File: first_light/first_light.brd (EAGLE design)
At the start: 100 x 50 mm, 50 parts, among them IC1 MC34063AD, J1 DCJ0202, J2 DCJ0202, Q1 ZXMN4A06GTA, T1 UM2222AU3T106, T2 UM2222AU3T106, T3 UM2222AU3T106, T4 UM2222AU3T106, T5 UM2222AU3T106, U1 ESP32-WROOM-32D

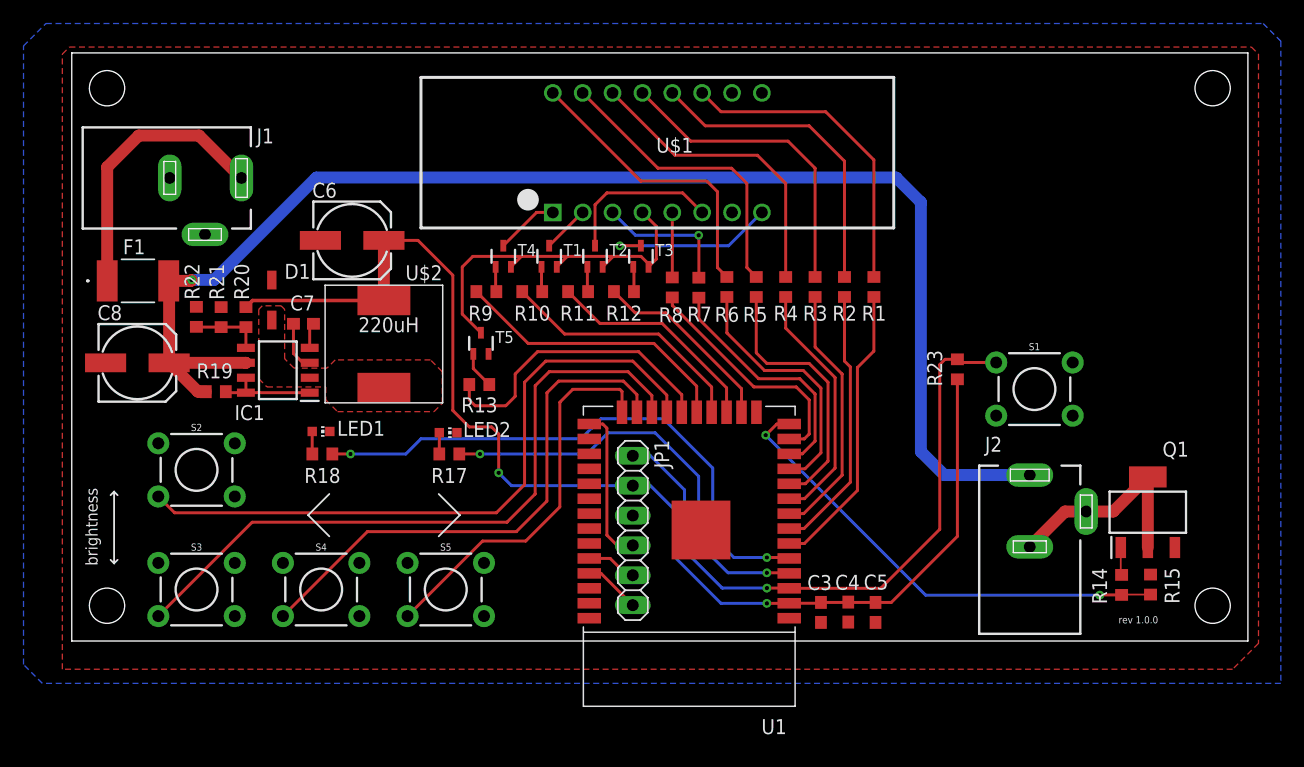
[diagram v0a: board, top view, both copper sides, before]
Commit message: added vias for a better ground plane and too fill between some tracks"
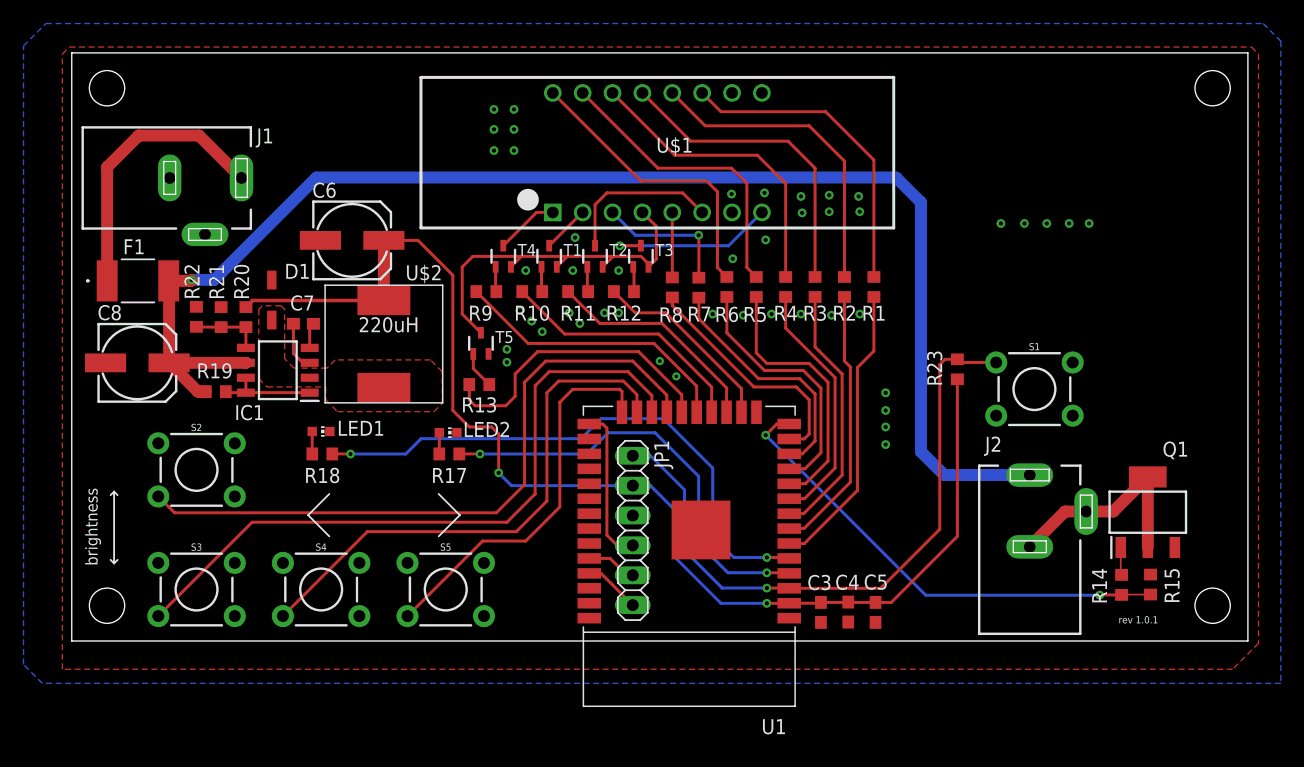
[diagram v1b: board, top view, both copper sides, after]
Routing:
- net GND: vias 0 -> 46
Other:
- board text added: "rev 1.0.1"
- board text removed: "rev 1.0.0"
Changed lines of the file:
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@@
 <text x="93.8" y="36.1" size="0.4064" layer="29">16 / 05 / 2022</text>
 <text x="76.3" y="29.4" size="3.81" layer="29">first light</text>
-<text x="89" y="1.5" size="0.6096" layer="25">rev 1.0.0</text>
+<text x="89" y="1.5" size="0.6096" layer="25">rev 1.0.1</text>
 </plain>
 <attributes>
@@
 </class>
 </classes>
-<designrules name="default">
+<designrules name="default *">
 <description language="de">&lt;b&gt;EAGLE Design Rules&lt;/b&gt;
 &lt;p&gt;
@@
 <param name="mdSmdStop" value="0mil"/>
 <param name="msWidth" value="6mil"/>
-<param name="msDrill" value="0.35mm"/>
+<param name="msDrill" value="0.3mm"/>
 <param name="msMicroVia" value="9.99mm"/>
 <param name="msBlindViaRatio" value="0.5"/>
@@
 <param name="mlMinCreamFrame" value="0mil"/>
 <param name="mlMaxCreamFrame" value="0mil"/>
-<param name="mlViaStopLimit" value="0mil"/>
+<param name="mlViaStopLimit" value="25mil"/>
 <param name="srRoundness" value="0"/>
 <param name="srMinRoundness" value="0mil"/>
@@
 <vertex x="-4.1" y="-2"/>
 </polygon>
+<via x="38.1" y="28.1" extent="1-16" drill="0.35"/>
+<via x="39.1" y="27.2" extent="1-16" drill="0.35"/>
+<via x="40" y="26.3" extent="1-16" drill="0.35"/>
+<via x="43.2" y="27" extent="1-16" drill="0.35"/>
+<via x="42.3" y="27.9" extent="1-16" drill="0.35"/>
+<via x="46.5" y="27.9" extent="1-16" drill="0.35"/>
+<via x="45.3" y="27.9" extent="1-16" drill="0.35"/>
+<via x="42.8" y="34.3" extent="1-16" drill="0.35"/>
+<via x="42.6" y="31.5" extent="1-16" drill="0.35"/>
+<via x="46.5" y="31.5" extent="1-16" drill="0.35"/>
+<via x="38.6" y="31.5" extent="1-16" drill="0.35"/>
+<via x="54.5" y="27.8" extent="1-16" drill="0.35"/>
+<via x="57.1" y="27.7" extent="1-16" drill="0.35"/>
+<via x="59.5" y="27.8" extent="1-16" drill="0.35"/>
+<via x="62" y="27.8" extent="1-16" drill="0.35"/>
+<via x="64.6" y="27.7" extent="1-16" drill="0.35"/>
+<via x="67" y="27.8" extent="1-16" drill="0.35"/>
+<via x="66.9" y="37.8" extent="1-16" drill="0.35"/>
+<via x="67" y="36.5" extent="1-16" drill="0.35"/>
+<via x="64.4" y="37.9" extent="1-16" drill="0.35"/>
+<via x="64.4" y="36.5" extent="1-16" drill="0.35"/>
+<via x="62" y="37.8" extent="1-16" drill="0.35"/>
+<via x="62.1" y="36.4" extent="1-16" drill="0.35"/>
+<via x="58.9" y="38.1" extent="1-16" drill="0.35"/>
+<via x="59" y="34.1" extent="1-16" drill="0.35"/>
+<via x="56.2" y="32.5" extent="1-16" drill="0.35"/>
+<via x="56.1" y="38" extent="1-16" drill="0.35"/>
+<via x="37.6" y="45.2" extent="1-16" drill="0.35"/>
+<via x="35.9" y="45.2" extent="1-16" drill="0.35"/>
+<via x="35.9" y="43.5" extent="1-16" drill="0.35"/>
+<via x="37.6" y="43.5" extent="1-16" drill="0.35"/>
+<via x="37.6" y="41.7" extent="1-16" drill="0.35"/>
+<via x="35.9" y="41.7" extent="1-16" drill="0.35"/>
+<via x="51.4" y="22.5" extent="1-16" drill="0.3"/>
+<via x="50" y="23.8" extent="1-16" drill="0.3"/>
+<via x="37" y="24.8" extent="1-16" drill="0.35"/>
+<via x="37" y="23.7" extent="1-16" drill="0.35"/>
+<via x="69.2" y="21.1" extent="1-16" drill="0.35"/>
+<via x="69.2" y="19.6" extent="1-16" drill="0.35"/>
+<via x="69.2" y="18.2" extent="1-16" drill="0.35"/>
+<via x="69.2" y="16.7" extent="1-16" drill="0.35"/>
+<via x="86.5" y="35.5" extent="1-16" drill="0.35"/>
+<via x="84.8" y="35.5" extent="1-16" drill="0.35"/>
+<via x="82.9" y="35.5" extent="1-16" drill="0.35"/>
+<via x="81" y="35.5" extent="1-16" drill="0.35"/>
+<via x="79" y="35.5" extent="1-16" drill="0.35"/>
 </signal>
 <signal name="SSD_BLANK">
